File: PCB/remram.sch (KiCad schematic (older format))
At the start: 0 parts

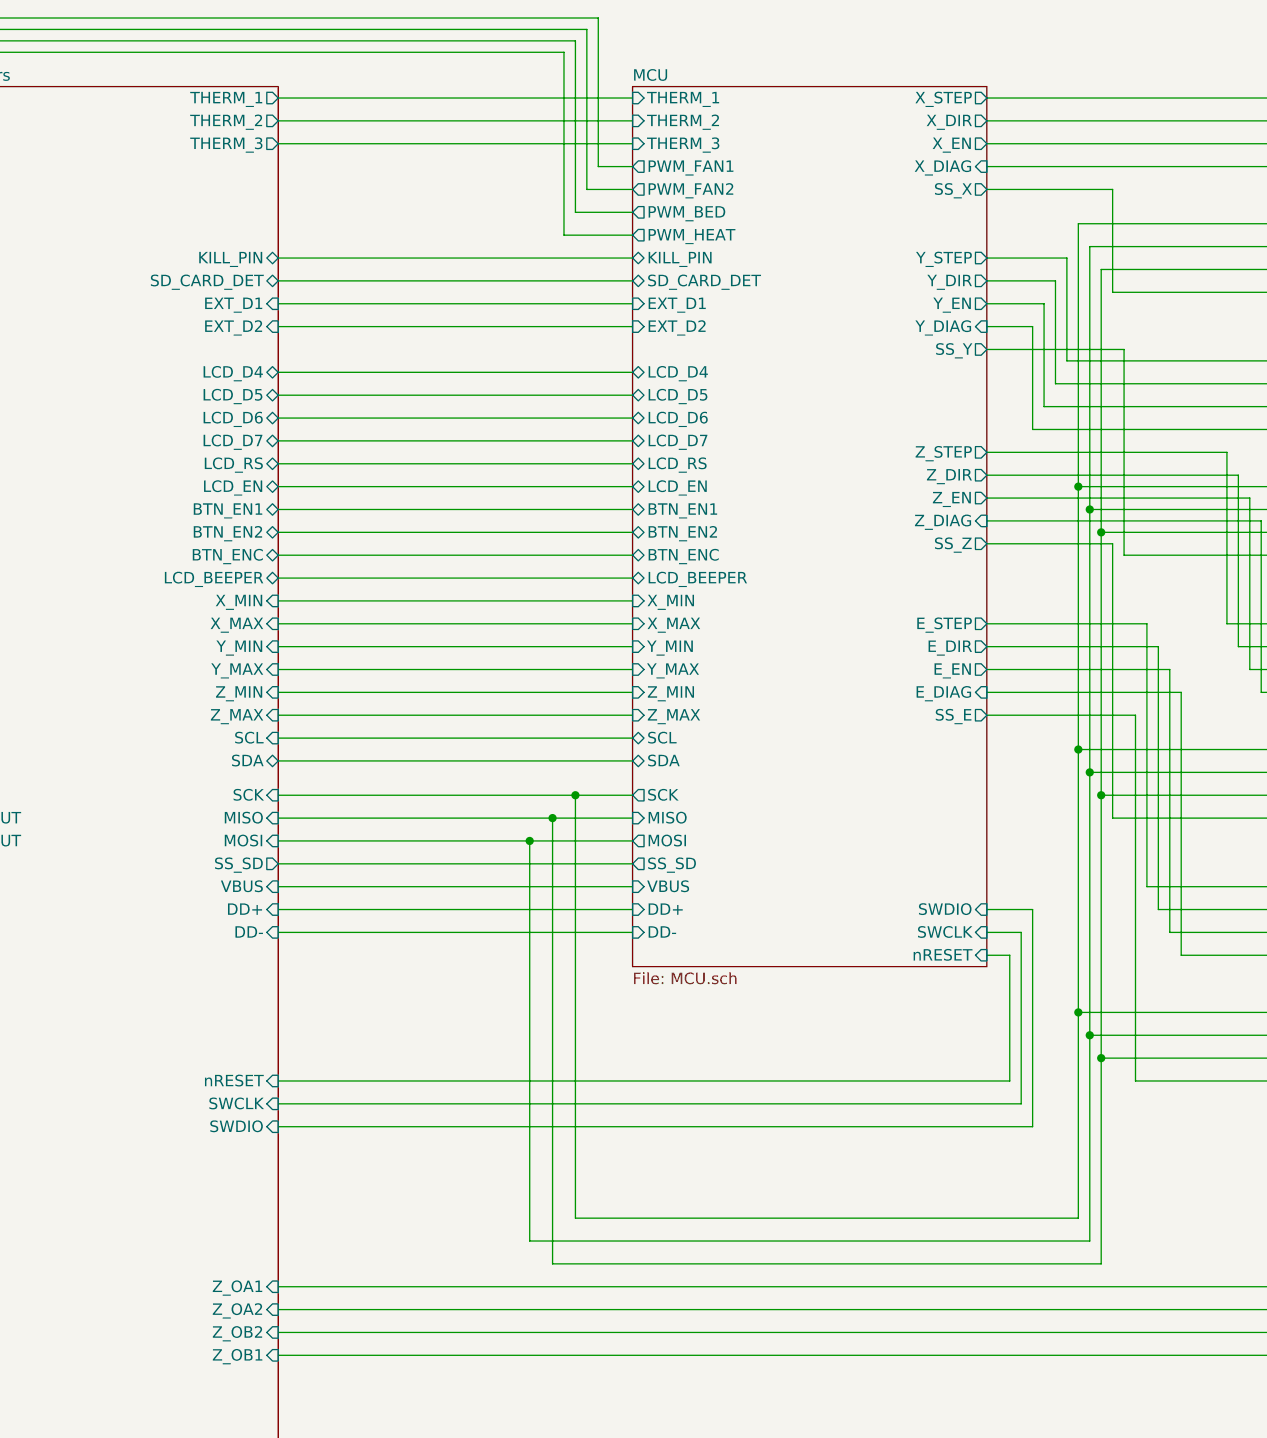
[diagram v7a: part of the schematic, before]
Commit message: First draft of RemRam.
I added a 20 pin expansion connector with the following pins:
 - SPI
 - I2C
 - USART
 - 4x PWM
 - 4x GPIO
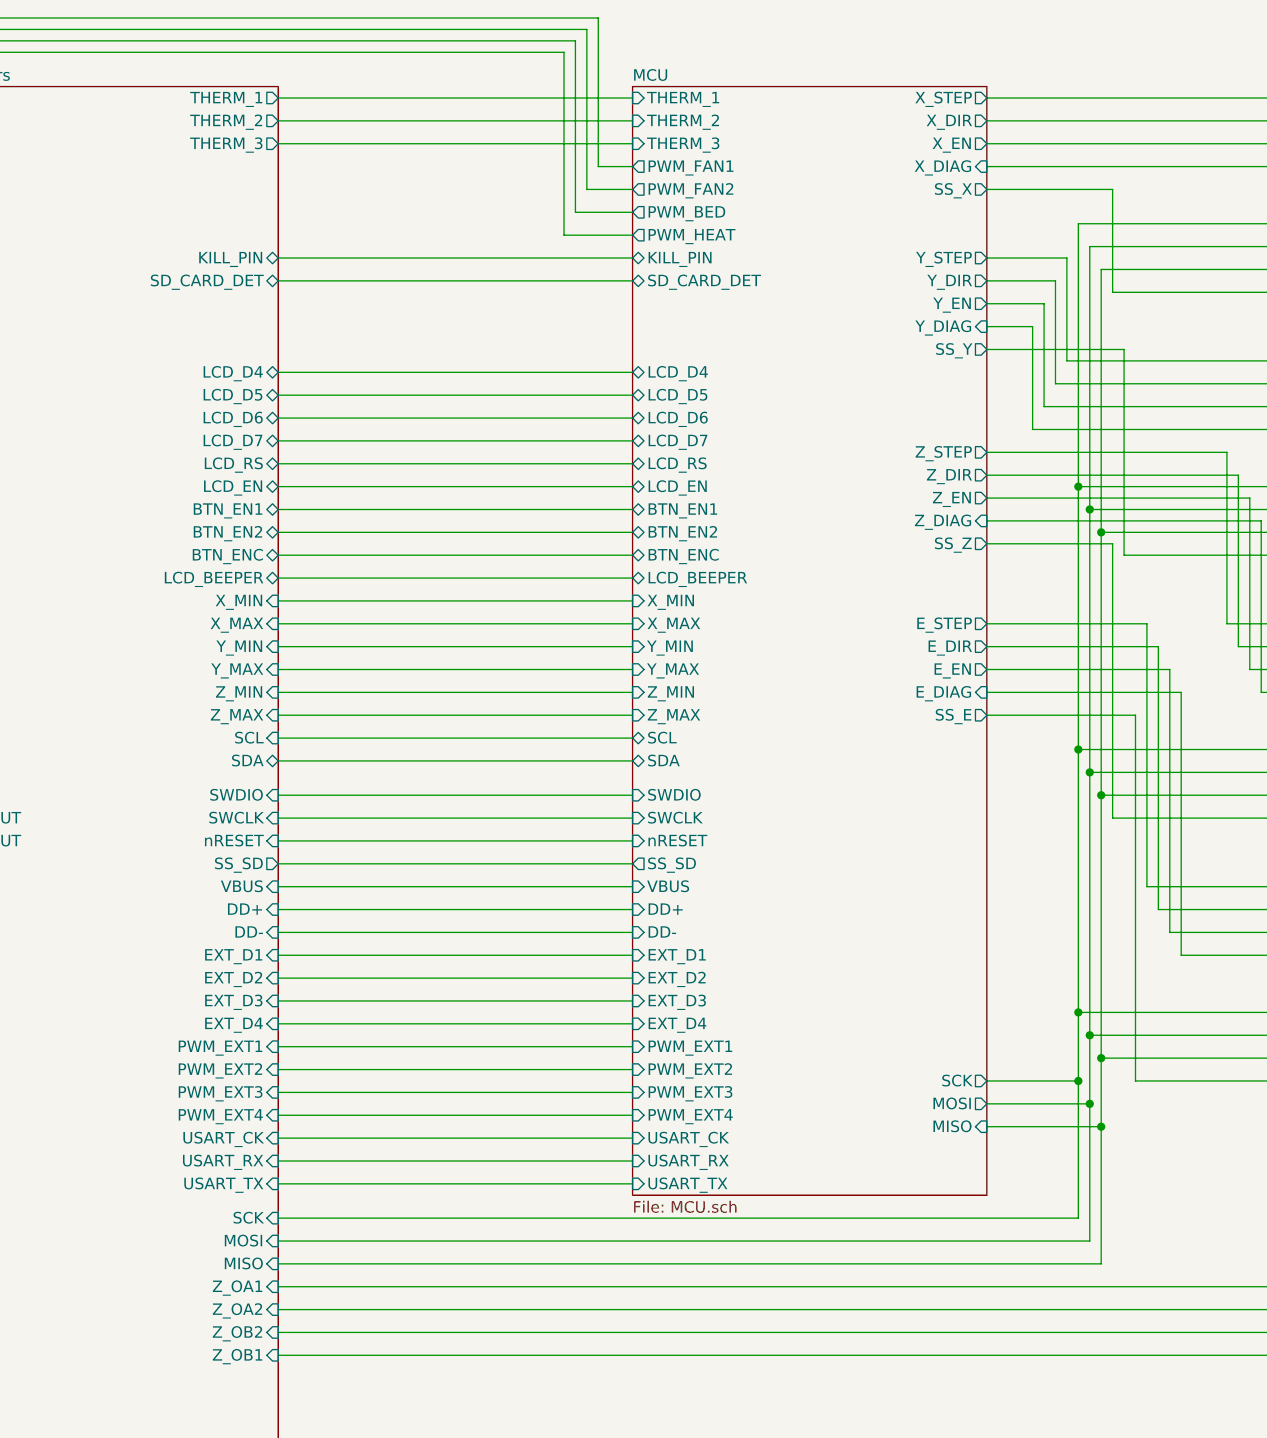
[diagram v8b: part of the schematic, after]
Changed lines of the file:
@@
 	6200 1700 4650 1700
 Wire Wire Line
-	4650 1800 6200 1800
-Wire Wire Line
-	6200 1900 4650 1900
-Wire Wire Line
 	6200 2100 4650 2100
 Wire Wire Line
@@
 	9100 1200 7750 1200
 Wire Wire Line
-	7750 4650 7850 4650
-Wire Wire Line
-	7850 4650 7850 5200
-Wire Wire Line
-	4650 5200 7850 5200
-Wire Wire Line
-	7750 4550 7900 4550
-Wire Wire Line
-	7900 4550 7900 5300
-Wire Wire Line
-	7900 5300 4650 5300
-Wire Wire Line
-	4650 5400 7950 5400
-Wire Wire Line
-	7950 5400 7950 4450
-Wire Wire Line
-	7950 4450 7750 4450
-Wire Wire Line
 	8150 1450 9100 1450
 Wire Wire Line
@@
 	9100 1750 8300 1750
 Wire Wire Line
-	8150 5800 8150 4900
-Wire Wire Line
-	8250 6000 8250 5100
+	8150 5800 8150 5200
+Wire Wire Line
+	8250 6000 8250 5400
 Wire Wire Line
 	9100 2900 8350 2900
@@
 Connection ~ 8200 5000
 Wire Wire Line
-	8200 5000 8200 5900
+	8200 5000 8200 5300
 Wire Wire Line
 	8200 3850 9100 3850
@@
 	6200 3800 4650 3800
 Wire Wire Line
-	4650 3950 5950 3950
-Wire Wire Line
-	6200 4050 5850 4050
-Wire Wire Line
-	4650 4150 5750 4150
-Wire Wire Line
-	6200 4250 4650 4250
-Wire Wire Line
 	4650 3600 6200 3600
 Wire Wire Line
@@
 Wire Wire Line
 	6200 2300 4650 2300
-Wire Wire Line
-	5950 3950 5950 5800
-Connection ~ 5950 3950
-Wire Wire Line
-	5950 3950 6200 3950
-Wire Wire Line
-	5950 5800 8150 5800
-Connection ~ 5850 4050
-Wire Wire Line
-	5850 4050 4650 4050
-Wire Wire Line
-	5750 4150 5750 5900
-Connection ~ 5750 4150
-Wire Wire Line
-	5750 4150 6200 4150
-Wire Wire Line
-	5850 6000 8250 6000
-Wire Wire Line
-	5750 5900 5850 5900
 Wire Wire Line
 	6200 4350 4650 4350
@@
 	8400 5200 9100 5200
 $Sheet
-S 6200 850  1550 3850
+S 6200 850  1550 4850
 U 5AD054EE
 F0 "MCU" 50
@@
 F26 "SCL" B L 6200 3700 50
 F27 "SDA" B L 6200 3800 50
-F28 "SWCLK" I R 7750 4550 50
-F29 "SWDIO" I R 7750 4450 50
+F28 "SWCLK" I L 6200 4050 50
+F29 "SWDIO" I L 6200 3950 50
 F30 "PWM_BED" O L 6200 1400 50
 F31 "PWM_HEAT" O L 6200 1500 50
-F32 "nRESET" I R 7750 4650 50
-F33 "SCK" O L 6200 3950 50
-F34 "MISO" I L 6200 4050 50
-F35 "MOSI" O L 6200 4150 50
+F32 "nRESET" I L 6200 4150 50
+F33 "SCK" O R 7750 5200 50
+F34 "MISO" I R 7750 5400 50
+F35 "MOSI" O R 7750 5300 50
 F36 "SS_X" O R 7750 1300 50
 F37 "SS_Y" O R 7750 2000 50
@@
 F43 "LCD_D6" B L 6200 2300 50
 F44 "LCD_D7" B L 6200 2400 50
-F45 "EXT_D1" I L 6200 1800 50
-F46 "EXT_D2" I L 6200 1900 50
+F45 "EXT_D1" I L 6200 4650 50
+F46 "EXT_D2" I L 6200 4750 50
 F47 "LCD_D5" B L 6200 2200 50
 F48 "LCD_D4" B L 6200 2100 50
@@
 F59 "Z_MAX" I L 6200 3600 50
 F60 "LCD_BEEPER" B L 6200 3000 50
+F61 "EXT_D4" I L 6200 4950 50
+F62 "EXT_D3" I L 6200 4850 50
+F63 "PWM_EXT2" I L 6200 5150 50
+F64 "PWM_EXT3" I L 6200 5250 50
+F65 "USART_RX" I L 6200 5550 50
+F66 "USART_TX" I L 6200 5650 50
+F67 "USART_CK" I L 6200 5450 50
+F68 "PWM_EXT4" I L 6200 5350 50
+F69 "PWM_EXT1" I L 6200 5050 50
 $EndSheet
 $Sheet
@@
 F3 "THERM_2" O R 4650 1000 50
 F4 "THERM_3" O R 4650 1100 50
-F5 "nRESET" I R 4650 5200 50
-F6 "SWDIO" I R 4650 5400 50
-F7 "SWCLK" I R 4650 5300 50
+F5 "nRESET" I R 4650 4150 50
+F6 "SWDIO" I R 4650 3950 50
+F7 "SWCLK" I R 4650 4050 50
 F8 "VBUS" I R 4650 4350 50
 F9 "DD+" I R 4650 4450 50
@@
 F30 "X_MAX" I R 4650 3200 50
 F31 "X_MIN" I R 4650 3100 50
-F32 "SCK" I R 4650 3950 50
-F33 "MISO" I R 4650 4050 50
-F34 "MOSI" I R 4650 4150 50
+F32 "SCK" I R 4650 5800 50
+F33 "MISO" I R 4650 6000 50
+F34 "MOSI" I R 4650 5900 50
 F35 "LCD_D6" B R 4650 2300 50
 F36 "LCD_D7" B R 4650 2400 50
-F37 "EXT_D1" I R 4650 1800 50
-F38 "EXT_D2" I R 4650 1900 50
+F37 "EXT_D1" I R 4650 4650 50
+F38 "EXT_D2" I R 4650 4750 50
 F39 "Z_OA1" I R 4650 6100 50
 F40 "Z_OA2" I R 4650 6200 50
 F41 "Z_OB2" I R 4650 6300 50
 F42 "Z_OB1" I R 4650 6400 50
+F43 "USART_TX" I R 4650 5650 50
+F44 "USART_RX" I R 4650 5550 50
+F45 "USART_CK" I R 4650 5450 50
+F46 "PWM_EXT1" I R 4650 5050 50
+F47 "PWM_EXT2" I R 4650 5150 50
+F48 "EXT_D3" I R 4650 4850 50
+F49 "EXT_D4" I R 4650 4950 50
+F50 "PWM_EXT3" I R 4650 5250 50
+F51 "PWM_EXT4" I R 4650 5350 50
 $EndSheet
 $Sheet
@@
 	11050 6400 4650 6400
 Wire Wire Line
-	5850 5900 8200 5900
-Wire Wire Line
 	11200 3750 10650 3750
 Wire Wire Line
@@
 	11050 4050 11050 6400
 Wire Wire Line
-	5850 4050 5850 6000
+	4650 4650 6200 4650
+Wire Wire Line
+	6200 4750 4650 4750
+Wire Wire Line
+	4650 4850 6200 4850
+Wire Wire Line
+	6200 4950 4650 4950
+Wire Wire Line
+	4650 5050 6200 5050
+Wire Wire Line
+	6200 5150 4650 5150
+Wire Wire Line
+	4650 5250 6200 5250
+Wire Wire Line
+	6200 5350 4650 5350
+Wire Wire Line
+	4650 5450 6200 5450
+Wire Wire Line
+	6200 5550 4650 5550
+Wire Wire Line
+	4650 5650 6200 5650
+Wire Wire Line
+	4650 3950 6200 3950
+Wire Wire Line
+	4650 4050 6200 4050
+Wire Wire Line
+	4650 4150 6200 4150
+Wire Wire Line
+	6200 4250 4650 4250
+Wire Wire Line
+	4650 5800 8150 5800
+Wire Wire Line
+	4650 5900 8200 5900
+Wire Wire Line
+	4650 6000 8250 6000
+Wire Wire Line
+	7750 5200 8150 5200
+Connection ~ 8150 5200
+Wire Wire Line
+	8150 5200 8150 4900
+Wire Wire Line
+	7750 5300 8200 5300
+Connection ~ 8200 5300
+Wire Wire Line
+	8200 5300 8200 5900
+Wire Wire Line
+	7750 5400 8250 5400
+Connection ~ 8250 5400
+Wire Wire Line
+	8250 5400 8250 5100
 $EndSCHEMATC
